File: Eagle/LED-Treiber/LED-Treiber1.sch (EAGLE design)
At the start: 13 parts, among them IC1 NE555, Q1 2N2907A, Q2 2N2907A, Q3 2N2907A, Q4 BUZ11

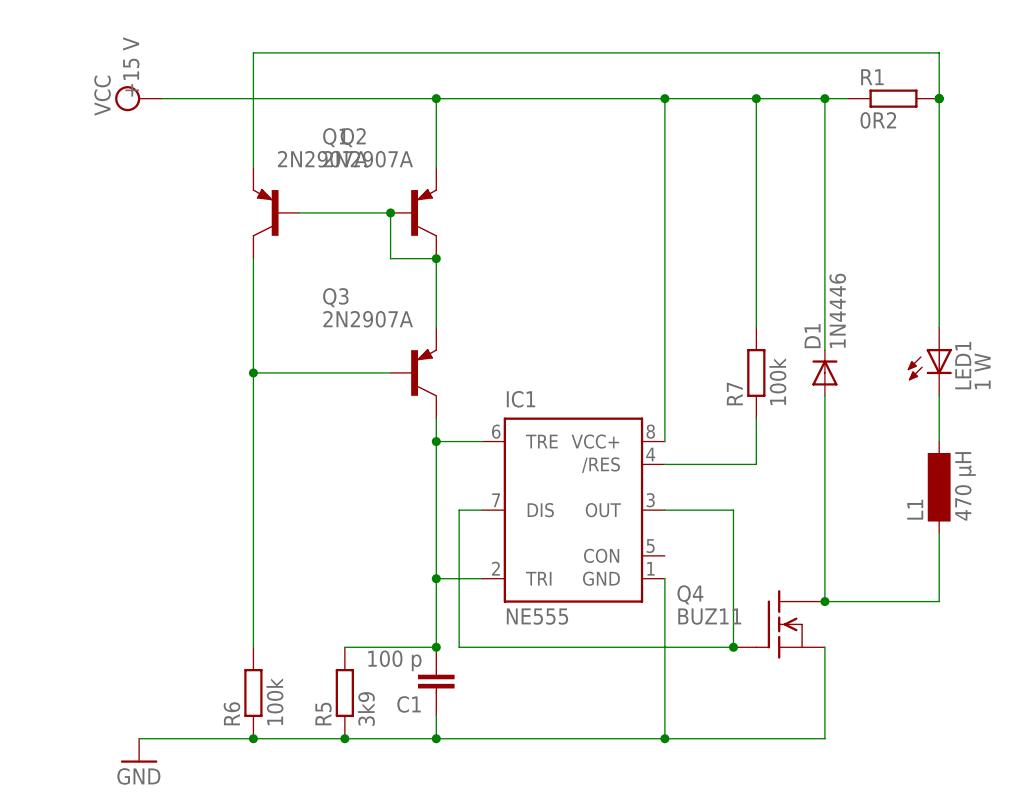
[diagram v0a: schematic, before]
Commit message: changed schematics - Measurement of current
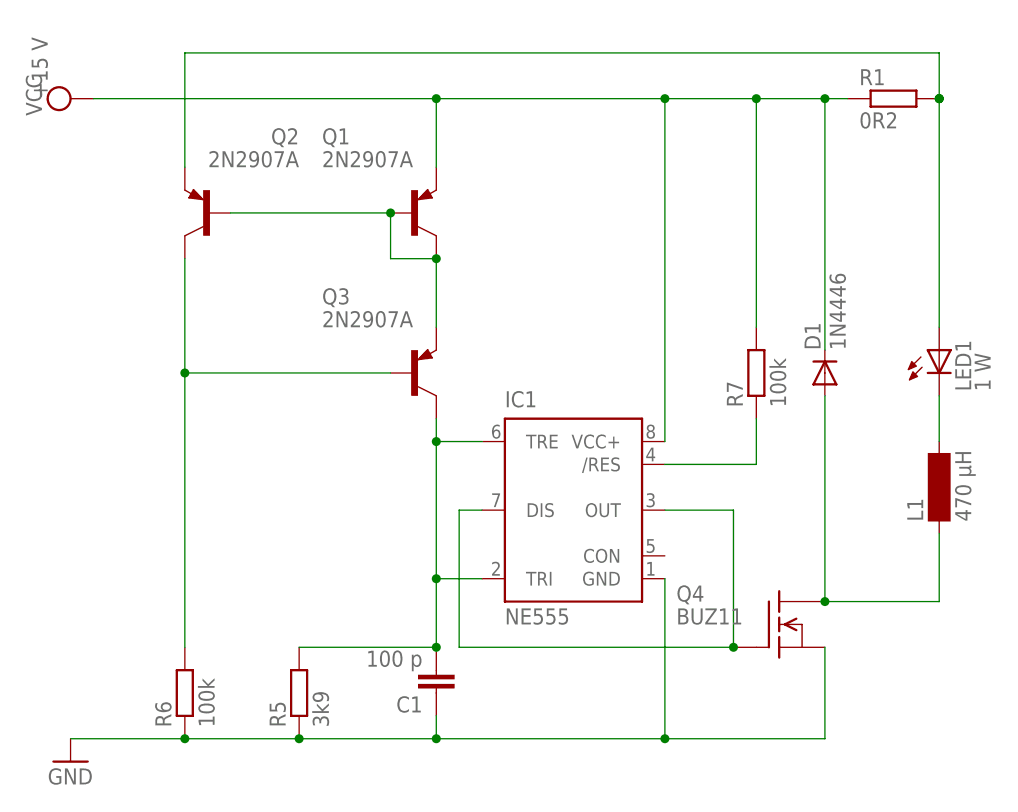
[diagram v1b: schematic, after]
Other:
- moved on the sheet: Q2, R5, R6
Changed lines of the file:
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@@
 <?xml version="1.0" encoding="utf-8"?>
 <!DOCTYPE eagle SYSTEM "eagle.dtd">
-<eagle version="6.2">
+<eagle version="9.6.2">
 <drawing>
 <settings>
 <setting alwaysvectorfont="no"/>
+<setting keepoldvectorfont="yes"/>
 <setting verticaltext="up"/>
 </settings>
@@
 </plain>
 <instances>
-<instance part="IC1" gate="G$1" x="43.18" y="60.96"/>
-<instance part="Q1" gate="G$1" x="25.4" y="93.98"/>
-<instance part="Q2" gate="G$1" x="10.16" y="93.98" rot="MR0"/>
-<instance part="Q3" gate="G$1" x="25.4" y="76.2"/>
-<instance part="C1" gate="G$1" x="27.94" y="40.64" rot="R180"/>
-<instance part="Q4" gate="G$1" x="66.04" y="48.26"/>
-<instance part="D1" gate="1" x="71.12" y="76.2" rot="R90"/>
-<instance part="L1" gate="G$1" x="83.82" y="63.5" rot="R90"/>
-<instance part="LED1" gate="G$1" x="83.82" y="78.74"/>
-<instance part="GND1" gate="1" x="-5.08" y="33.02"/>
-<instance part="SUPPLY1" gate="G$1" x="-5.08" y="106.68" rot="R90">
-<attribute name="VCC" x="-5.08" y="106.68" size="1.778" layer="96" rot="R90"/>
-</instance>
-<instance part="R5" gate="G$1" x="17.78" y="40.64" rot="R90"/>
-<instance part="R6" gate="G$1" x="7.62" y="40.64" rot="R90"/>
-<instance part="R7" gate="G$1" x="63.5" y="76.2" rot="R90"/>
-<instance part="R1" gate="G$1" x="78.74" y="106.68"/>
+<instance part="IC1" gate="G$1" x="43.18" y="60.96" smashed="yes">
+<attribute name="NAME" x="35.56" y="72.39" size="1.778" layer="95"/>
+<attribute name="VALUE" x="35.56" y="48.26" size="1.778" layer="96"/>
+</instance>
+<instance part="Q1" gate="G$1" x="25.4" y="93.98" smashed="yes">
+<attribute name="NAME" x="15.24" y="101.6" size="1.778" layer="95"/>
+<attribute name="VALUE" x="15.24" y="99.06" size="1.778" layer="96"/>
+</instance>
+<instance part="Q2" gate="G$1" x="2.54" y="93.98" smashed="yes" rot="MR0">
+<attribute name="NAME" x="12.7" y="101.6" size="1.778" layer="95" rot="MR0"/>
+<attribute name="VALUE" x="12.7" y="99.06" size="1.778" layer="96" rot="MR0"/>
+</instance>
+<instance part="Q3" gate="G$1" x="25.4" y="76.2" smashed="yes">
+<attribute name="NAME" x="15.24" y="83.82" size="1.778" layer="95"/>
+<attribute name="VALUE" x="15.24" y="81.28" size="1.778" layer="96"/>
+</instance>
+<instance part="C1" gate="G$1" x="27.94" y="40.64" smashed="yes" rot="R180">
+<attribute name="NAME" x="26.416" y="40.259" size="1.778" layer="95" rot="R180"/>
+<attribute name="VALUE" x="26.416" y="45.339" size="1.778" layer="96" rot="R180"/>
+</instance>
+<instance part="Q4" gate="G$1" x="66.04" y="48.26" smashed="yes">
+<attribute name="VALUE" x="54.61" y="48.26" size="1.778" layer="96"/>
+<attribute name="NAME" x="54.61" y="50.8" size="1.778" layer="95"/>
+</instance>
+<instance part="D1" gate="1" x="71.12" y="76.2" smashed="yes" rot="R90">
+<attribute name="NAME" x="70.6374" y="78.74" size="1.778" layer="95" rot="R90"/>
+<attribute name="VALUE" x="73.4314" y="78.74" size="1.778" layer="96" rot="R90"/>
+</instance>
+<instance part="L1" gate="G$1" x="83.82" y="63.5" smashed="yes" rot="R90">
+<attribute name="NAME" x="82.042" y="59.69" size="1.778" layer="95" rot="R90"/>
+<attribute name="VALUE" x="87.376" y="59.69" size="1.778" layer="96" rot="R90"/>
+</instance>
+<instance part="LED1" gate="G$1" x="83.82" y="78.74" smashed="yes">
+<attribute name="NAME" x="87.376" y="74.168" size="1.778" layer="95" rot="R90"/>
+<attribute name="VALUE" x="89.535" y="74.168" size="1.778" layer="96" rot="R90"/>
+</instance>
+<instance part="GND1" gate="1" x="-12.7" y="33.02" smashed="yes">
+<attribute name="VALUE" x="-15.24" y="30.48" size="1.778" layer="96"/>
+</instance>
+<instance part="SUPPLY1" gate="G$1" x="-12.7" y="106.68" smashed="yes" rot="R90">
+<attribute name="VCC" x="-15.24" y="106.68" size="1.778" layer="96" rot="R90"/>
+<attribute name="VALUE" x="-15.875" y="104.775" size="1.778" layer="96" rot="R90"/>
+</instance>
+<instance part="R5" gate="G$1" x="12.7" y="40.64" smashed="yes" rot="R90">
+<attribute name="NAME" x="11.2014" y="36.83" size="1.778" layer="95" rot="R90"/>
+<attribute name="VALUE" x="16.002" y="36.83" size="1.778" layer="96" rot="R90"/>
+</instance>
+<instance part="R6" gate="G$1" x="0" y="40.64" smashed="yes" rot="R90">
+<attribute name="NAME" x="-1.4986" y="36.83" size="1.778" layer="95" rot="R90"/>
+<attribute name="VALUE" x="3.302" y="36.83" size="1.778" layer="96" rot="R90"/>
+</instance>
+<instance part="R7" gate="G$1" x="63.5" y="76.2" smashed="yes" rot="R90">
+<attribute name="NAME" x="62.0014" y="72.39" size="1.778" layer="95" rot="R90"/>
+<attribute name="VALUE" x="66.802" y="72.39" size="1.778" layer="96" rot="R90"/>
+</instance>
+<instance part="R1" gate="G$1" x="78.74" y="106.68" smashed="yes">
+<attribute name="NAME" x="74.93" y="108.1786" size="1.778" layer="95"/>
+<attribute name="VALUE" x="74.93" y="103.378" size="1.778" layer="96"/>
+</instance>
 </instances>
 <busses>
@@
 <wire x1="22.86" y1="88.9" x2="27.94" y2="88.9" width="0.1524" layer="91"/>
 <wire x1="27.94" y1="88.9" x2="27.94" y2="81.28" width="0.1524" layer="91"/>
-<wire x1="12.7" y1="93.98" x2="22.86" y2="93.98" width="0.1524" layer="91"/>
+<wire x1="5.08" y1="93.98" x2="22.86" y2="93.98" width="0.1524" layer="91"/>
 <junction x="22.86" y="93.98"/>
 <junction x="27.94" y="88.9"/>
@@
 <wire x1="33.02" y1="53.34" x2="27.94" y2="53.34" width="0.1524" layer="91"/>
 <wire x1="27.94" y1="53.34" x2="27.94" y2="45.72" width="0.1524" layer="91"/>
-<wire x1="27.94" y1="45.72" x2="17.78" y2="45.72" width="0.1524" layer="91"/>
+<wire x1="27.94" y1="45.72" x2="12.7" y2="45.72" width="0.1524" layer="91"/>
 <junction x="27.94" y="68.58"/>
 <junction x="27.94" y="53.34"/>
@@
 <net name="N$3" class="0">
 <segment>
-<wire x1="7.62" y1="88.9" x2="7.62" y2="76.2" width="0.1524" layer="91"/>
-<wire x1="7.62" y1="76.2" x2="7.62" y2="45.72" width="0.1524" layer="91"/>
-<wire x1="22.86" y1="76.2" x2="7.62" y2="76.2" width="0.1524" layer="91"/>
-<junction x="7.62" y="76.2"/>
+<wire x1="0" y1="88.9" x2="0" y2="76.2" width="0.1524" layer="91"/>
+<wire x1="0" y1="76.2" x2="0" y2="45.72" width="0.1524" layer="91"/>
+<wire x1="22.86" y1="76.2" x2="0" y2="76.2" width="0.1524" layer="91"/>
+<junction x="0" y="76.2"/>
 <pinref part="Q2" gate="G$1" pin="C"/>
 <pinref part="Q3" gate="G$1" pin="B"/>
@@
 <wire x1="83.82" y1="111.76" x2="83.82" y2="106.68" width="0.1524" layer="91"/>
 <wire x1="83.82" y1="106.68" x2="83.82" y2="81.28" width="0.1524" layer="91"/>
-<wire x1="83.82" y1="111.76" x2="7.62" y2="111.76" width="0.1524" layer="91"/>
-<wire x1="7.62" y1="111.76" x2="7.62" y2="99.06" width="0.1524" layer="91"/>
+<wire x1="83.82" y1="111.76" x2="0" y2="111.76" width="0.1524" layer="91"/>
+<wire x1="0" y1="111.76" x2="0" y2="99.06" width="0.1524" layer="91"/>
 <junction x="83.82" y="106.68"/>
 <junction x="83.82" y="106.68"/>
@@
 <net name="GND" class="0">
 <segment>
-<wire x1="17.78" y1="35.56" x2="27.94" y2="35.56" width="0.1524" layer="91"/>
+<wire x1="12.7" y1="35.56" x2="27.94" y2="35.56" width="0.1524" layer="91"/>
 <wire x1="27.94" y1="38.1" x2="27.94" y2="35.56" width="0.1524" layer="91"/>
 <wire x1="27.94" y1="35.56" x2="53.34" y2="35.56" width="0.1524" layer="91"/>
@@
 <wire x1="53.34" y1="35.56" x2="71.12" y2="35.56" width="0.1524" layer="91"/>
 <wire x1="71.12" y1="35.56" x2="71.12" y2="45.72" width="0.1524" layer="91"/>
-<wire x1="17.78" y1="35.56" x2="7.62" y2="35.56" width="0.1524" layer="91"/>
-<wire x1="7.62" y1="35.56" x2="-5.08" y2="35.56" width="0.1524" layer="91"/>
+<wire x1="12.7" y1="35.56" x2="0" y2="35.56" width="0.1524" layer="91"/>
+<wire x1="0" y1="35.56" x2="-12.7" y2="35.56" width="0.1524" layer="91"/>
 <junction x="27.94" y="35.56"/>
 <junction x="53.34" y="35.56"/>
-<junction x="17.78" y="35.56"/>
-<junction x="7.62" y="35.56"/>
+<junction x="12.7" y="35.56"/>
+<junction x="0" y="35.56"/>
 <pinref part="C1" gate="G$1" pin="1"/>
 <pinref part="IC1" gate="G$1" pin="GND"/>
@@
 <wire x1="63.5" y1="106.68" x2="63.5" y2="81.28" width="0.1524" layer="91"/>
 <wire x1="53.34" y1="68.58" x2="53.34" y2="106.68" width="0.1524" layer="91"/>
-<wire x1="27.94" y1="106.68" x2="-2.54" y2="106.68" width="0.1524" layer="91"/>
+<wire x1="27.94" y1="106.68" x2="-10.16" y2="106.68" width="0.1524" layer="91"/>
 <wire x1="71.12" y1="78.74" x2="71.12" y2="106.68" width="0.1524" layer="91"/>
 <wire x1="71.12" y1="106.68" x2="63.5" y2="106.68" width="0.1524" layer="91"/>
